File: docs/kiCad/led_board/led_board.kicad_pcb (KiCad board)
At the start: 2 copper layers, 10.2 x 62.2 mm, 8 parts, among them J1 Conn_01x03, J2 Conn_01x03, J3 Conn_01x01, J4 Conn_01x01

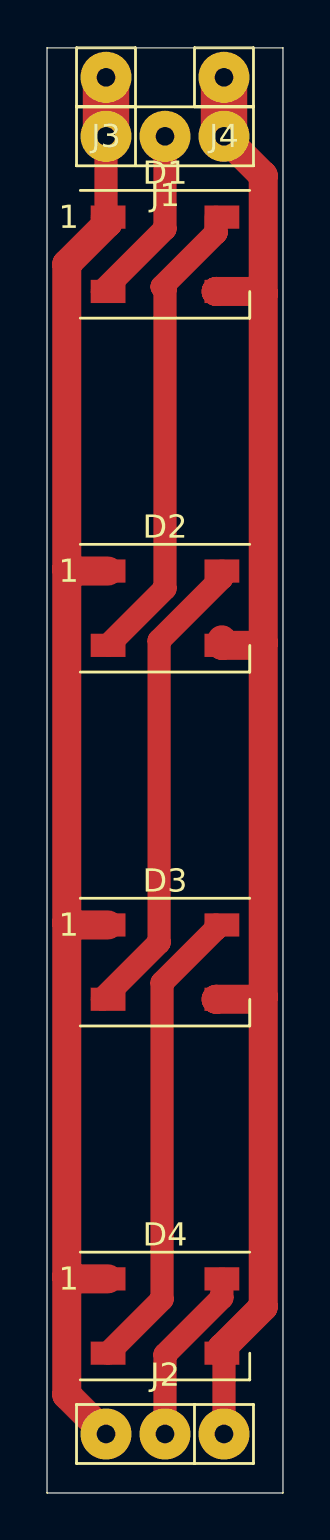
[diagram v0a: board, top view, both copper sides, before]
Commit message: bilgeAlarm led_board v2
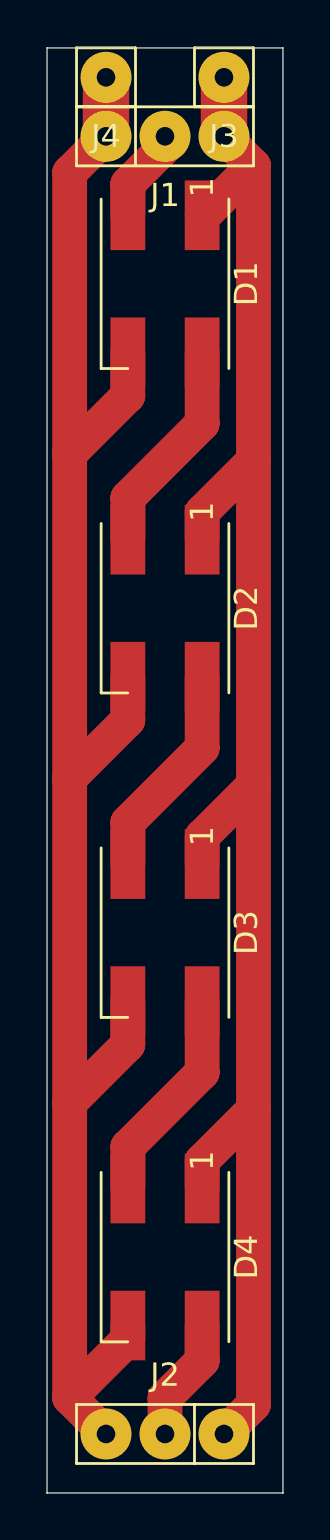
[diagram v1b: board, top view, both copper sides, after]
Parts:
- D1, D2, D3, D4: footprint LED_SMD:LED_WS2812B_PLCC4_5.0x5.0mm_P3.2mm -> cnc3018-PCB:myWS2812
- moved J3 5.08 mm to (7.62, -61.0)
- moved J4 5.08 mm to (2.54, -61.0)
- moved D4 2.54 mm to (5.08, -10.2), turned to 270 degrees
- moved D1 1.27 mm to (5.08, -52.1), turned to 270 degrees
- moved D3 1.27 mm to (5.08, -24.1), turned to 270 degrees
- turned D2 to 270 degrees
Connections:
- J1 pad 1: Net-(D1-Pad1) -> Net-(D1-Pad3)
- J1 pad 3: Net-(D1-Pad3) -> Net-(D1-Pad1)
- J2 pad 1: Net-(D1-Pad3) -> Net-(D1-Pad1)
- J2 pad 3: Net-(D1-Pad1) -> Net-(D1-Pad3)
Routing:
- net Net-(D1-Pad3): track 66.1 -> 80.1 mm
- net Net-(D2-Pad4): track 20.6 -> 9.40 mm
- net Net-(D1-Pad4): track 20.5 -> 9.40 mm
- net Net-(D3-Pad4): track 20.4 -> 9.40 mm
- net Net-(D1-Pad1): track 65.4 -> 75.5 mm
- net Net-(D1-Pad2): track 7.80 -> 4.06 mm
- net Net-(D4-Pad4): track 7.69 -> 5.33 mm
